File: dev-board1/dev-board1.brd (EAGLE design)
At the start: 100 x 80 mm, 87 parts, among them IC1 MSP432E401, IC2 MT48LC16M16A2, IC3 SIM800C, IC4 CC3100MOD-LWK, IC5 TPD3E001DRL, IC6 TPD3E001DRL, IC7 TPD3E001DRL, J1 MAGJACK, J2 SIM-78723-1001, J3 ER-TFT024-3, J4 SWD_SHROUD, U3 ER-TFT024-3-OUTLINE, X2 BU-SMA-V

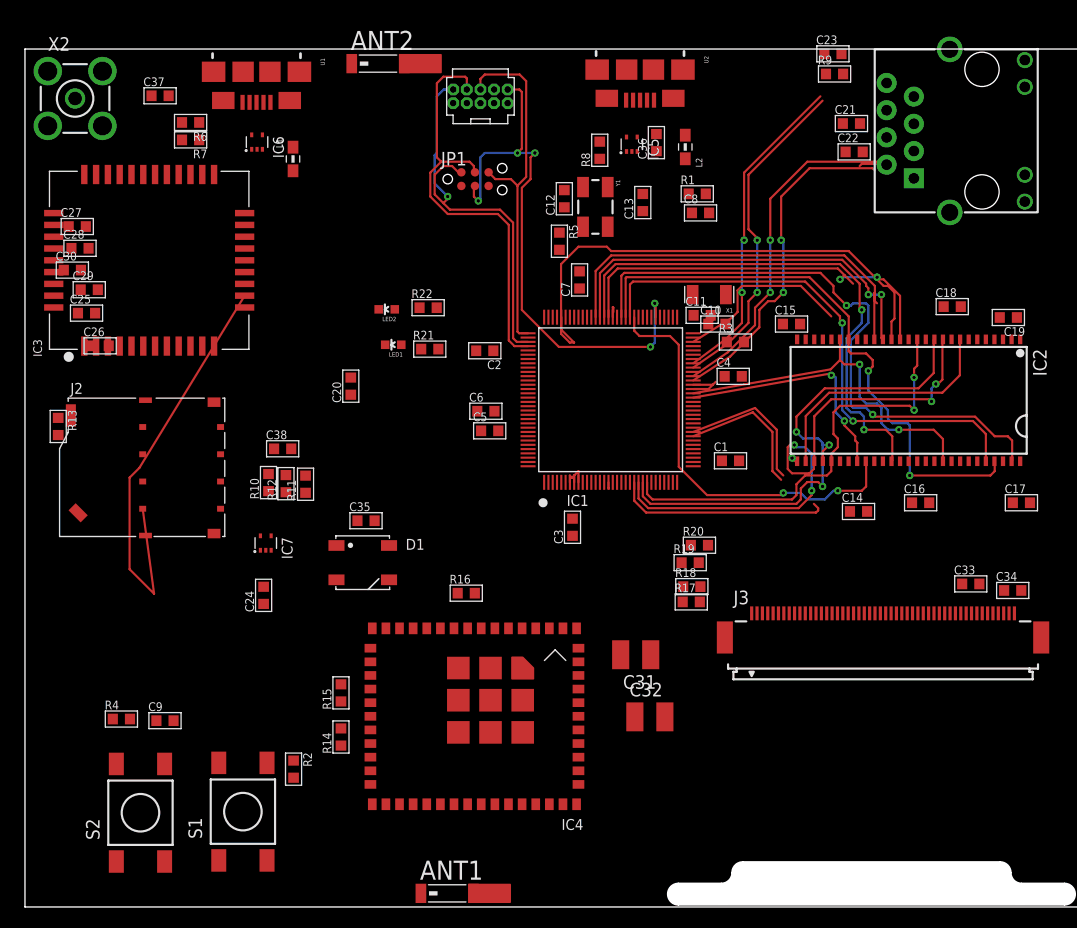
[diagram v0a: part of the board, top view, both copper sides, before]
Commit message: adding power supply
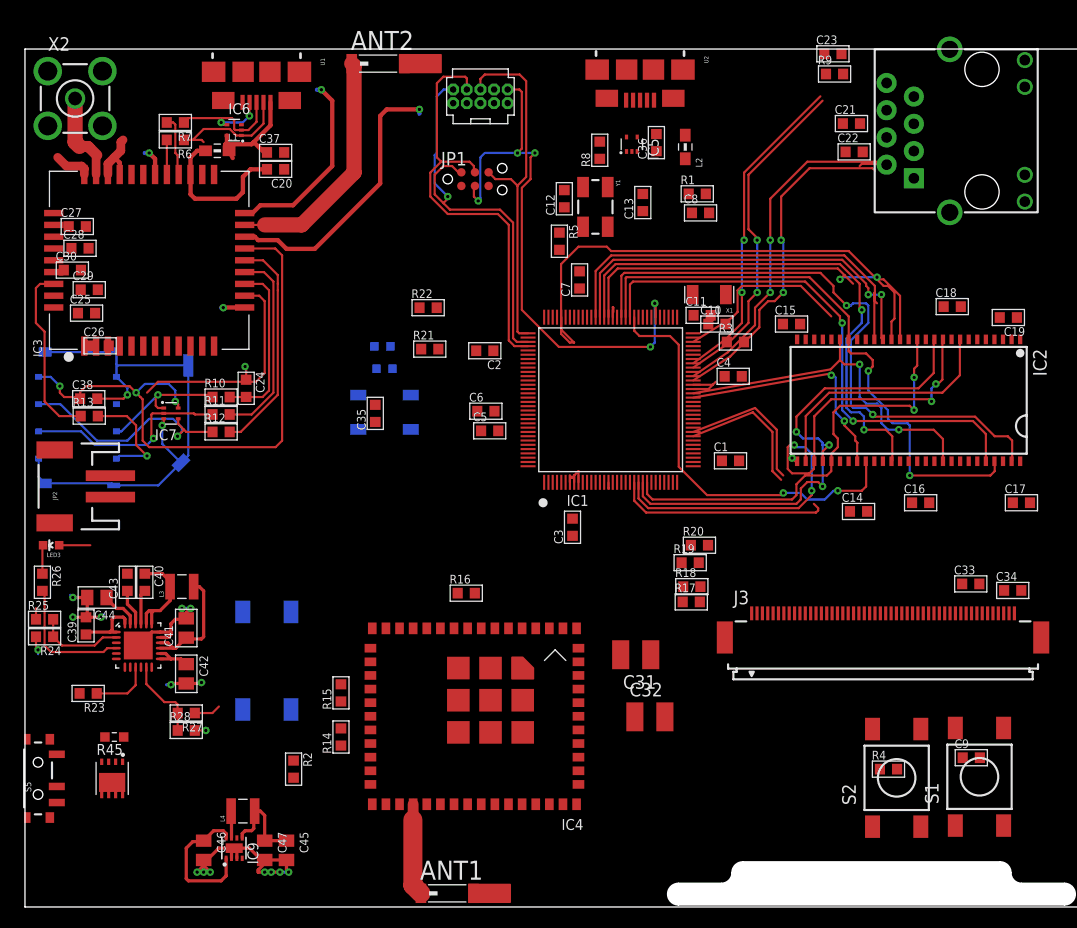
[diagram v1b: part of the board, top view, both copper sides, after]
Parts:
- added C39: 1u, passives-7351:C0603-N
- added C40: 47n, passives-7351:C0603-N
- added C41, C42, C44: 10u, passives-7351:C0805-N
- added C43: 4.7u, passives-7351:C0603-N
- added C45, C46, C47: 0805/10u/10V/X5R, TiLDA Mk3 Parts:C0805-N
- added IC8: BQ25601, TiLDA Mk4 Parts:QFN-24
- added IC9: TPS62082, TiLDA Mk3 Parts:WSON8
- added JP2: (no value), TiLDA Mk4 Parts:JST-2-SMD
- added L3: (no value), TiLDA Mk4 Parts:1008
- added L4: SRN2512-2R2M, TiLDA Mk3 Parts:1008
- added LED3: red, TiLDA Mk4 Parts:LED-0603
- added Q6: CSD25402Q3A, TiLDA Mk3 Parts:Q3A
- added R23, R25: 2k, passives-7351:R0603-N
- added R24: dnp, passives-7351:R0603-N
- added R26: 4.7k, passives-7351:R0603-N
- added R27, R28: 10k, passives-7351:R0603-N
- added R45: 0603/220k/5%, TiLDA Mk3 Parts:C0603K-SMALL
- added S3: (no value), Switches:6MMTACTSM
- added S5: CUS-12TB, TiLDA Mk3 Parts:SWITCH-SPST-SMD-A
- moved C9 75.3 mm to (88.2, 13.9)
- moved R4 71.7 mm to (80.5, 12.9)
- moved S2 70.6 mm to (81.3, 12.0)
- moved S1 68.8 mm to (89.0, 12.1)
- moved C20 21.4 mm to (23.4, 68.8), turned to 180 degrees
- moved C24 19.4 mm to (20.6, 48.4), turned to 270 degrees
- moved C38 18.7 mm to (5.94, 47.4)
- moved J2 16.4 mm to (1.88, 45.6), flipped to the bottom
- moved IC7 15.0 mm to (13.6, 46.0), turned to 270 degrees
- moved D1 14.2 mm to (33.5, 46.1), flipped to the bottom
- moved C37 12.0 mm to (23.4, 70.4)
- moved R11 10.2 mm to (18.3, 45.9), turned to 0 degrees
- moved C35 10.0 mm to (32.7, 46.0), turned to 90 degrees
- moved R10 9.12 mm to (18.3, 47.5), turned to 0 degrees
- moved R12 7.74 mm to (18.3, 44.3), turned to 0 degrees
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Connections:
- new net N$3: C42.1, IC8.13, IC8.14, JP2.2
- new net N$63: C40.1, IC8.19, IC8.20, L3.1
- new net N$73: C40.2, IC8.21
- new net N$74: C43.1, IC8.22, R27.1
- new net N$75: C44.1, IC8.23
- new net N$76: IC8.12, S3.3, S3.4
- new net N$78: IC8.9, R23.1
- new net N$79: IC8.2, R24.1, R25.2
- new net N$80: IC8.5
- new net N$81: IC8.6
- new net N$82: IC8.7
- new net N$83: IC8.4, R26.2
- new net N$84: LED3.C, R26.1
- new net N$85: IC8.3
- new net N$86: IC8.11, R27.2, R28.1
- new net SW: IC9.7, L4.1
- new net VABT_SWTICHED: Q6.1, Q6.2, Q6.3
- new net VBAT: Q6.5, Q6.6, Q6.7, Q6.8, Q6.EP, R45.1
- new net VBAT_SWITCH_CONTROL: Q6.4, R45.2, S5.3
- new net V_UNREG: C41.1, C46.1, IC8.15, IC8.16, IC9.1, IC9.8, L3.2, R25.1
- net +3V3: now also C45.1, C47.1, IC9.5, L4.2
- net GND: now also C39.2, C41.2, C42.2, C43.2, C44.2, C45.2, C46.2, C47.2, IC8.17, IC8.18, IC9.2, IC9.3, IC9.EP, JP2.1, R23.2, R24.2, R28.2, S3.1, S3.2, S5.2
- net USB_VBUS: now also C39.1, IC8.1, IC8.24, LED3.A
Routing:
- net GND: track 2.42 -> 157.2 mm, vias 1 -> 24
- net N$35: track 0.00 -> 56.7 mm, vias 0 -> 3
- net V_UNREG: track 0.00 -> 25.8 mm
- net N$62: track 0.00 -> 22.5 mm
- net N$32: track 0.00 -> 21.8 mm, vias 0 -> 1
- net N$29: track 0.00 -> 20.7 mm
- net N$31: track 0.00 -> 19.6 mm, vias 0 -> 1
- net N$28: track 0.00 -> 18.3 mm
- net N$34: track 0.00 -> 16.7 mm
- net N$27: track 0.00 -> 15.8 mm
- net N$18: track 0.00 -> 14.4 mm
- net N$30: track 0.00 -> 12.4 mm, vias 0 -> 1
- net N$83: track 0.00 -> 12.3 mm
- net N$10: track 0.00 -> 11.6 mm
- net N$19: track 0.00 -> 11.0 mm
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
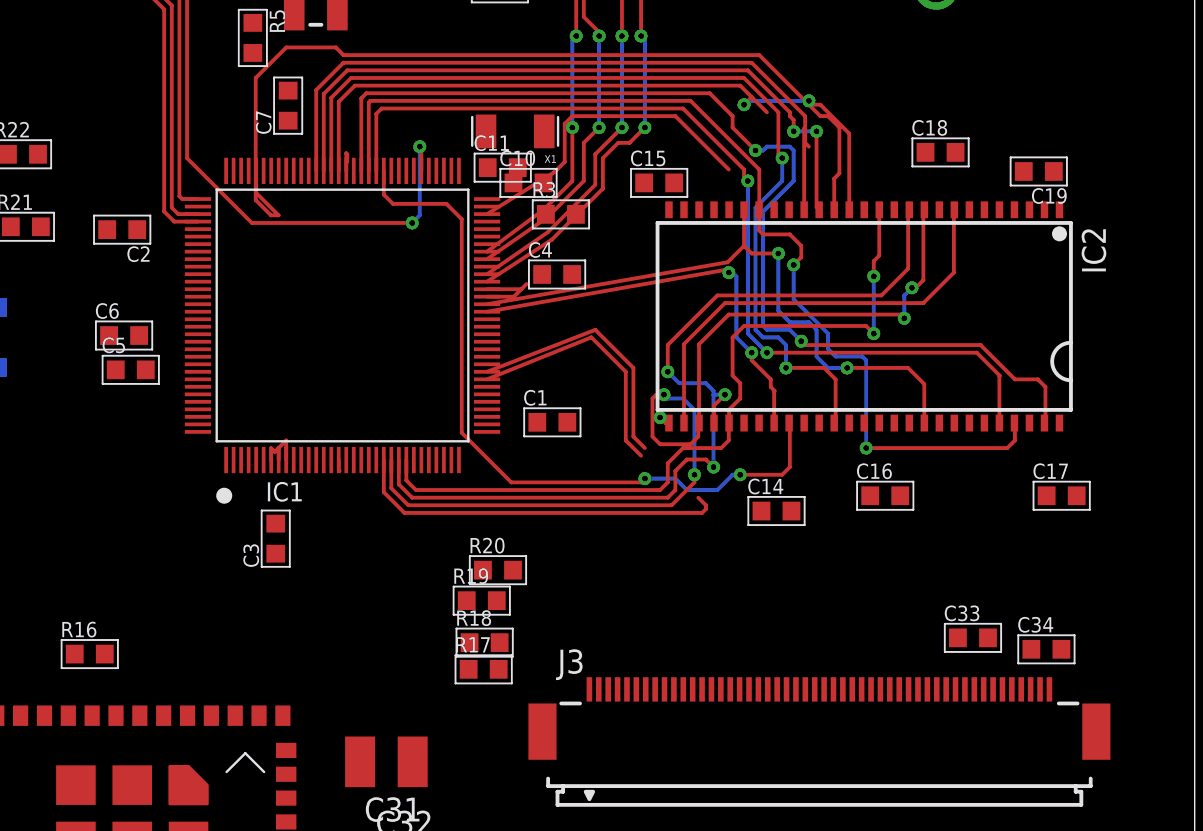
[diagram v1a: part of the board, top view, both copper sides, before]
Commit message: connecting some serial interfaces
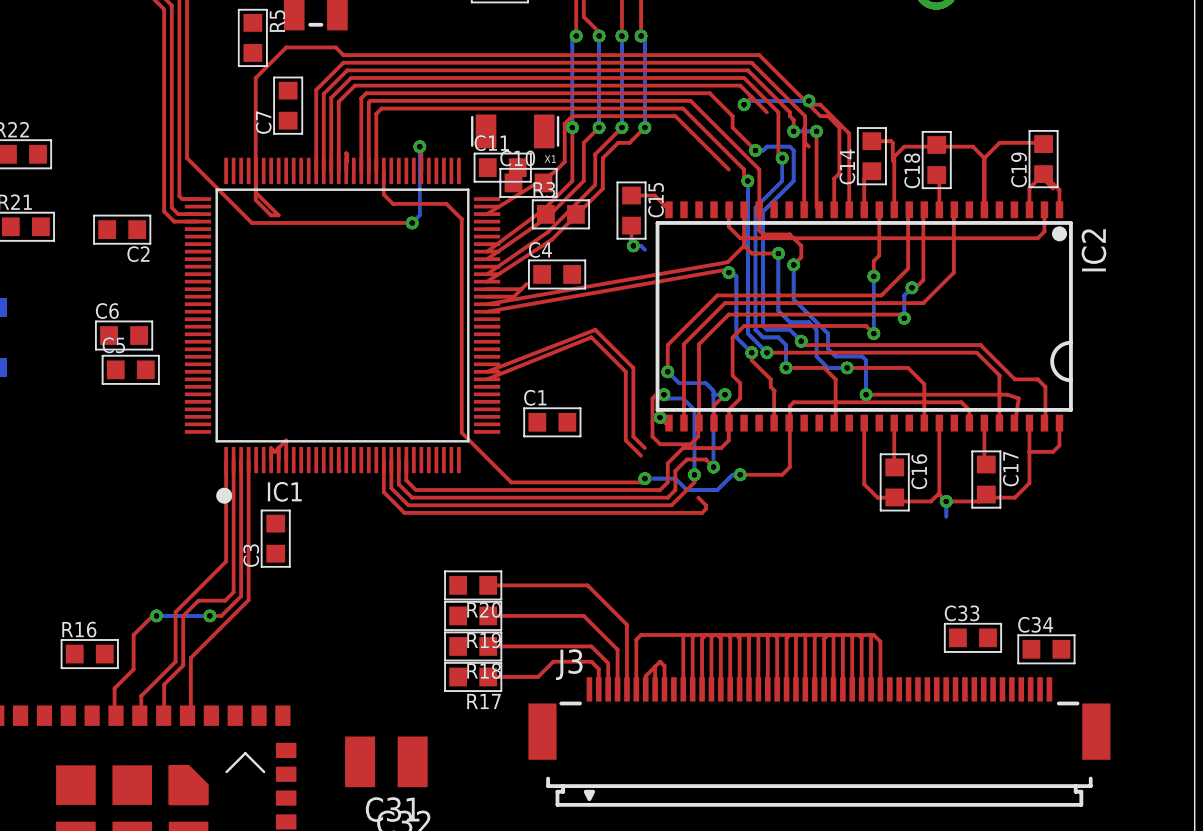
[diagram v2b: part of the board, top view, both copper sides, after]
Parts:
- moved C14 19.6 mm to (82.8, 55.8), turned to 90 degrees
- moved C17 4.11 mm to (88.9, 38.6), turned to 270 degrees
- moved C15 2.08 mm to (70.0, 52.9), turned to 270 degrees
- moved R20 1.55 mm to (61.6, 32.9), turned to 180 degrees
- moved R19 0.93 mm to (61.6, 31.3), turned to 180 degrees
- moved C16 0.87 mm to (84.0, 38.4), turned to 270 degrees
- moved C19 0.71 mm to (91.9, 55.6), turned to 90 degrees
- moved R17 0.69 mm to (61.6, 28.0), turned to 180 degrees
- moved R18 0.64 mm to (61.6, 29.7), turned to 180 degrees
- moved C18 0.45 mm to (86.3, 55.6), turned to 90 degrees
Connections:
- removed net N$25: IC4.46
- removed net N$26: IC4.47
- removed net N$46: IC3.1
- removed net N$47: IC3.2
- removed net N$50: IC4.5
- removed net N$51: IC4.6
- removed net N$52: IC4.7
- removed net N$53: IC4.8
- removed net N$64: J3.33
- removed net N$65: J3.34
- new net CC_CLK: IC1.4, IC4.5
- new net CC_CS: IC1.3, IC4.8
- new net CC_MISO: IC1.1, IC4.7
- new net CC_MOSI: IC1.2, IC4.6
- new net CC_RX: IC1.126, IC4.47
- new net CC_TX: IC1.125, IC4.46
- new net LCD_CLK: IC1.35
- new net LCD_CS: IC1.36
- new net LCD_MISO: IC1.38, J3.33
- new net LCD_MOSI: IC1.37, J3.34
- new net N$72: IC1.18
- new net SIM_RX: IC1.117, IC3.2
- new net SIM_TX: IC1.116, IC3.1
- net S0: now also IC1.29
- net S1: now also IC1.30
- net S2: now also IC1.31
- net S29: now also IC1.103
- net S3: now also IC1.32
- net S30: now also IC1.104
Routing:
- net GND: track 157.2 -> 282.6 mm, vias 24 -> 26
- net +3V3: track 17.1 -> 38.2 mm
- net S0: track 0.00 -> 19.3 mm
- net CC_CS: track 0.00 -> 18.6 mm, vias 0 -> 2
- net CC_MOSI: track 0.00 -> 16.0 mm
- net CC_MISO: track 0.00 -> 15.5 mm
- net CC_CLK: track 0.00 -> 15.0 mm
- net N$59: track 0.00 -> 11.7 mm
- net S12: track 39.1 -> 50.5 mm
- net N$58: track 0.00 -> 9.75 mm
- net N$57: track 0.00 -> 8.16 mm
- net N$56: track 0.00 -> 7.47 mm
- net S14: track 54.2 -> 51.9 mm

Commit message: some more connections done
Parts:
- added C48: 10p, passives-7351:C0603-N
- added C49: 33p, passives-7351:C0603-N
- added C50: 4.7u, passives-7351:C0603-N
- added C51: 100u, TiLDA Mk4 Parts:C1210
- added LED4: red, TiLDA Mk4 Parts:LED-0603
- added Q2, Q3, Q4: (no value), TiLDA Mk4 Parts:SOT23-3
- added R29: 10k, passives-7351:R0603-N
- added R30: 2k, passives-7351:R0603-N
- added S4: (no value), Switches:6MMTACTSM
- added U$1: MIC9.7MM, SparkFun-Sensors:MIC-9.7MM
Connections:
- removed net N$66: J3.38
- new net N$25: IC3.41, Q4.1, R29.2
- new net N$26: J3.36
- new net N$46: LED4.C, Q4.3
- new net N$52: Q2.1
- new net N$53: IC3.39, Q3.3, S4.3, S4.4
- new net N$64: LED4.A, R30.1
- new net N$65: Q3.1
- net +3V3: now also R30.2
- net GND: now also C48.1, C49.1, C50.1, C51.2, Q2.2, Q3.2, Q4.2, R29.1, S4.1, S4.2
- net LCD_CLK: now also J3.37
- net LCD_CS: now also J3.38
- net N$45: now also C48.2, C49.2, C50.2, C51.1
- net N$60: now also Q2.3
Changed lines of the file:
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@@
 </element>
 <element name="R45" library="TiLDA Mk3 Parts" package="C0603K-SMALL" value="0603/220k/5%" x="8.3312" y="15.8496" rot="R180"/>
+<element name="U$1" library="SparkFun-Sensors" package="MIC-9.7MM" value="MIC9.7MM" x="23.7744" y="37.3888">
+<attribute name="PROD_ID" value="COMP-08856" x="23.7744" y="37.3888" size="1.778" layer="27" display="off"/>
+</element>
+<element name="C48" library="passives-7351" package="C0603-N" value="10p" x="-5.2832" y="-10.3632"/>
+<element name="C49" library="passives-7351" package="C0603-N" value="33p" x="-5.2832" y="-13.4112"/>
+<element name="C50" library="passives-7351" package="C0603-N" value="4.7u" x="-5.2832" y="-16.4592"/>
+<element name="C51" library="TiLDA Mk4 Parts" package="C1210" value="100u" x="-4.8768" y="-21.1328"/>
+<element name="Q2" library="TiLDA Mk4 Parts" package="SOT23-3" value="" x="-12.192" y="-23.1648"/>
+<element name="Q3" library="TiLDA Mk4 Parts" package="SOT23-3" value="" x="-15.24" y="-23.1648"/>
+<element name="S4" library="Switches" package="6MMTACTSM" value="" x="-10.9728" y="-30.48"/>
+<element name="Q4" library="TiLDA Mk4 Parts" package="SOT23-3" value="" x="-18.288" y="-39.624"/>
+<element name="R29" library="passives-7351" package="R0603-N" value="10k" x="-17.6784" y="-43.2816"/>
+<element name="LED4" library="TiLDA Mk4 Parts" package="LED-0603" value="red" x="-21.5392" y="-42.672"/>
+<element name="R30" library="passives-7351" package="R0603-N" value="2k" x="-20.5232" y="-46.3296"/>
 </elements>
 <signals>
@@
 <wire x1="72.76" y1="27.38" x2="72.76" y2="30.2624" width="0.2032" layer="1"/>
 <wire x1="72.76" y1="30.2624" x2="72.7456" y2="30.2768" width="0.2032" layer="1"/>
+<contactref element="C50" pad="1"/>
+<contactref element="C51" pad="2"/>
+<contactref element="C49" pad="1"/>
+<contactref element="C48" pad="1"/>
+<contactref element="Q2" pad="2"/>
+<contactref element="Q3" pad="2"/>
+<contactref element="S4" pad="2"/>
+<contactref element="S4" pad="1"/>
+<contactref element="Q4" pad="2"/>
+<contactref element="R29" pad="1"/>
 <wire x1="76.2888" y1="77.6732" x2="74.5364" y2="79.5528" width="0" layer="19" extent="1-1"/>
 <wire x1="76.2636" y1="73.0504" x2="76.2888" y2="77.6732" width="0" layer="19" extent="1-1"/>
@@
 <wire x1="79.03" y1="7.4896" x2="86.7516" y2="7.5912" width="0" layer="19" extent="1-1"/>
 <wire x1="83.9976" y1="52.924" x2="82.3976" y2="41.564" width="0" layer="19" extent="1-1"/>
+<wire x1="-6.0832" y1="-10.3632" x2="2.9692" y2="11.2388" width="0" layer="19" extent="1-1"/>
+<wire x1="-6.0832" y1="-13.4112" x2="-6.0832" y2="-10.3632" width="0" layer="19" extent="1-1"/>
+<wire x1="-6.0832" y1="-16.4592" x2="-6.0832" y2="-13.4112" width="0" layer="19" extent="1-1"/>
+<wire x1="-3.4768" y1="-21.1328" x2="-6.0832" y2="-16.4592" width="0" layer="19" extent="1-1"/>
+<wire x1="-6.4228" y1="-28.23" x2="-3.4768" y2="-21.1328" width="0" layer="19" extent="1-1"/>
+<wire x1="-11.242" y1="-24.1648" x2="-6.4228" y2="-28.23" width="0" layer="19" extent="1-1"/>
+<wire x1="-14.29" y1="-24.1648" x2="-11.242" y2="-24.1648" width="0" layer="19" extent="1-1"/>
+<wire x1="-15.5228" y1="-28.23" x2="-14.29" y2="-24.1648" width="0" layer="19" extent="1-1"/>
+<wire x1="-17.338" y1="-40.624" x2="-15.5228" y2="-28.23" width="0" layer="19" extent="1-1"/>
+<wire x1="-18.4784" y1="-43.2816" x2="-17.338" y2="-40.624" width="0" layer="19" extent="1-1"/>
 </signal>
 <signal name="N$2">
@@
 <wire x1="70.76" y1="27.38" x2="70.76" y2="28.088" width="0.2032" layer="1"/>
 <wire x1="70.76" y1="28.088" x2="71.26" y2="28.588" width="0.2032" layer="1"/>
+<contactref element="R30" pad="2"/>
 <wire x1="77.8636" y1="73.0504" x2="80.345" y2="74.295" width="0" layer="19" extent="1-1"/>
 <wire x1="78.1176" y1="70.4088" x2="77.8636" y2="73.0504" width="0" layer="19" extent="1-1"/>
@@
 <wire x1="21.9456" y1="8.9408" x2="25.0444" y2="12.0524" width="0" layer="19" extent="1-1"/>
 <wire x1="39.9288" y1="74.9554" x2="50.81" y2="54.9948" width="0" layer="19" extent="1-1"/>
+<wire x1="-19.7232" y1="-46.3296" x2="20.2572" y2="6.4364" width="0" layer="19" extent="1-1"/>
 </signal>
 <signal name="N$7">
@@
 <contactref element="IC3" pad="34"/>
 <contactref element="IC3" pad="35"/>
+<contactref element="C51" pad="1"/>
+<contactref element="C50" pad="2"/>
+<contactref element="C48" pad="2"/>
+<contactref element="C49" pad="2"/>
 <wire x1="2.6824" y1="63.5996" x2="2.6824" y2="64.6996" width="0" layer="19" extent="1-1"/>
+<wire x1="-4.4832" y1="-10.3632" x2="2.6824" y2="63.5996" width="0" layer="19" extent="1-1"/>
+<wire x1="-4.4832" y1="-13.4112" x2="-4.4832" y2="-10.3632" width="0" layer="19" extent="1-1"/>
+<wire x1="-4.4832" y1="-16.4592" x2="-4.4832" y2="-13.4112" width="0" layer="19" extent="1-1"/>
+<wire x1="-6.2768" y1="-21.1328" x2="-4.4832" y2="-16.4592" width="0" layer="19" extent="1-1"/>
 </signal>
 <signal name="SIM_TX">
@@
 <contactref element="R19" pad="2"/>
 <contactref element="R18" pad="2"/>
+<contactref element="Q2" pad="3"/>
 <wire x1="60.7696" y1="31.2928" x2="60.7696" y2="32.9184" width="0" layer="19" extent="1-1"/>
 <wire x1="60.7696" y1="29.6672" x2="60.7696" y2="31.2928" width="0" layer="19" extent="1-1"/>
 <wire x1="60.7696" y1="28.0416" x2="60.7696" y2="29.6672" width="0" layer="19" extent="1-1"/>
+<wire x1="-12.192" y1="-22.0648" x2="60.7696" y2="28.0416" width="0" layer="19" extent="1-1"/>
 </signal>
 <signal name="N$61">
 <contactref element="J3" pad="10"/>
-</signal>
-<signal name="N$66">
-<contactref element="J3" pad="38"/>
 </signal>
 <signal name="N$67">
@@
 <signal name="LCD_CLK">
 <contactref element="IC1" pad="35"/>
+<contactref element="J3" pad="37"/>
+<wire x1="62.31" y1="41.8948" x2="85.76" y2="27.38" width="0" layer="19" extent="1-1"/>
 </signal>
 <signal name="LCD_CS">
 <contactref element="IC1" pad="36"/>
+<contactref element="J3" pad="38"/>
+<wire x1="62.31" y1="42.2948" x2="86.26" y2="27.38" width="0" layer="19" extent="1-1"/>
 </signal>
 <signal name="LCD_MISO">
@@
 <wire x1="42.4688" y1="26.0562" x2="42.545" y2="25.98" width="0.2032" layer="1"/>
 </signal>
+<signal name="N$26">
+<contactref element="J3" pad="36"/>
+</signal>
+<signal name="N$52">
+<contactref element="Q2" pad="1"/>
+</signal>
+<signal name="N$53">
+<contactref element="IC3" pad="39"/>
+<contactref element="Q3" pad="3"/>
+<contactref element="S4" pad="3"/>
+<contactref element="S4" pad="4"/>
+<wire x1="-15.24" y1="-22.0648" x2="2.6824" y2="59.1996" width="0" layer="19" extent="1-1"/>
+<wire x1="-15.5228" y1="-32.73" x2="-15.24" y2="-22.0648" width="0" layer="19" extent="1-1"/>
+<wire x1="-6.4228" y1="-32.73" x2="-15.5228" y2="-32.73" width="0" layer="19" extent="1-1"/>
+</signal>
+<signal name="N$25">
+<contactref element="IC3" pad="41"/>
+<contactref element="Q4" pad="1"/>
+<contactref element="R29" pad="2"/>
+<wire x1="-19.238" y1="-40.624" x2="2.6824" y2="56.9996" width="0" layer="19" extent="1-1"/>
+<wire x1="-16.8784" y1="-43.2816" x2="-19.238" y2="-40.624" width="0" layer="19" extent="1-1"/>
+</signal>
+<signal name="N$46">
+<contactref element="Q4" pad="3"/>
+<contactref element="LED4" pad="C"/>
+<wire x1="-18.288" y1="-38.524" x2="-21.5392" y2="-41.922" width="0" layer="19" extent="1-1"/>
+</signal>
+<signal name="N$64">
+<contactref element="LED4" pad="A"/>
+<contactref element="R30" pad="1"/>
+<wire x1="-21.5392" y1="-43.422" x2="-21.3232" y2="-46.3296" width="0" layer="19" extent="1-1"/>
+</signal>
+<signal name="N$65">
+<contactref element="Q3" pad="1"/>
+</signal>
 </signals>

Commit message: adding magjack
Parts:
- added JP3, JP4, JP5: (no value), TiLDA Mk4 Parts:1X02
- J1: value MAGJACK -> MAGJACK-RJMG16XXX-8; device SparkFun-Connectors:MAGJACK -> TiLDA Mk4 Parts:RJMG163118101NR
- moved J1 21.1 mm to (79.9, 69.7)
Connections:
- net +3V3: now also J1.1, JP3.1, JP3.2; no longer J1.3
- net N$20: now also J1.5; no longer J1.2
- net N$21: now also J1.4; no longer J1.1
- net N$22: now also J1.3; no longer J1.8
- net N$23: now also J1.2; no longer J1.7
- net N$24: now also J1.TAB1, J1.TAB2; no longer J1.M1, J1.M2
- net V_UNREG: now also JP4.1, JP5.1
